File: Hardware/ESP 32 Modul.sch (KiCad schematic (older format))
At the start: 23 parts, among them U401 ESP32-WROOM-32U

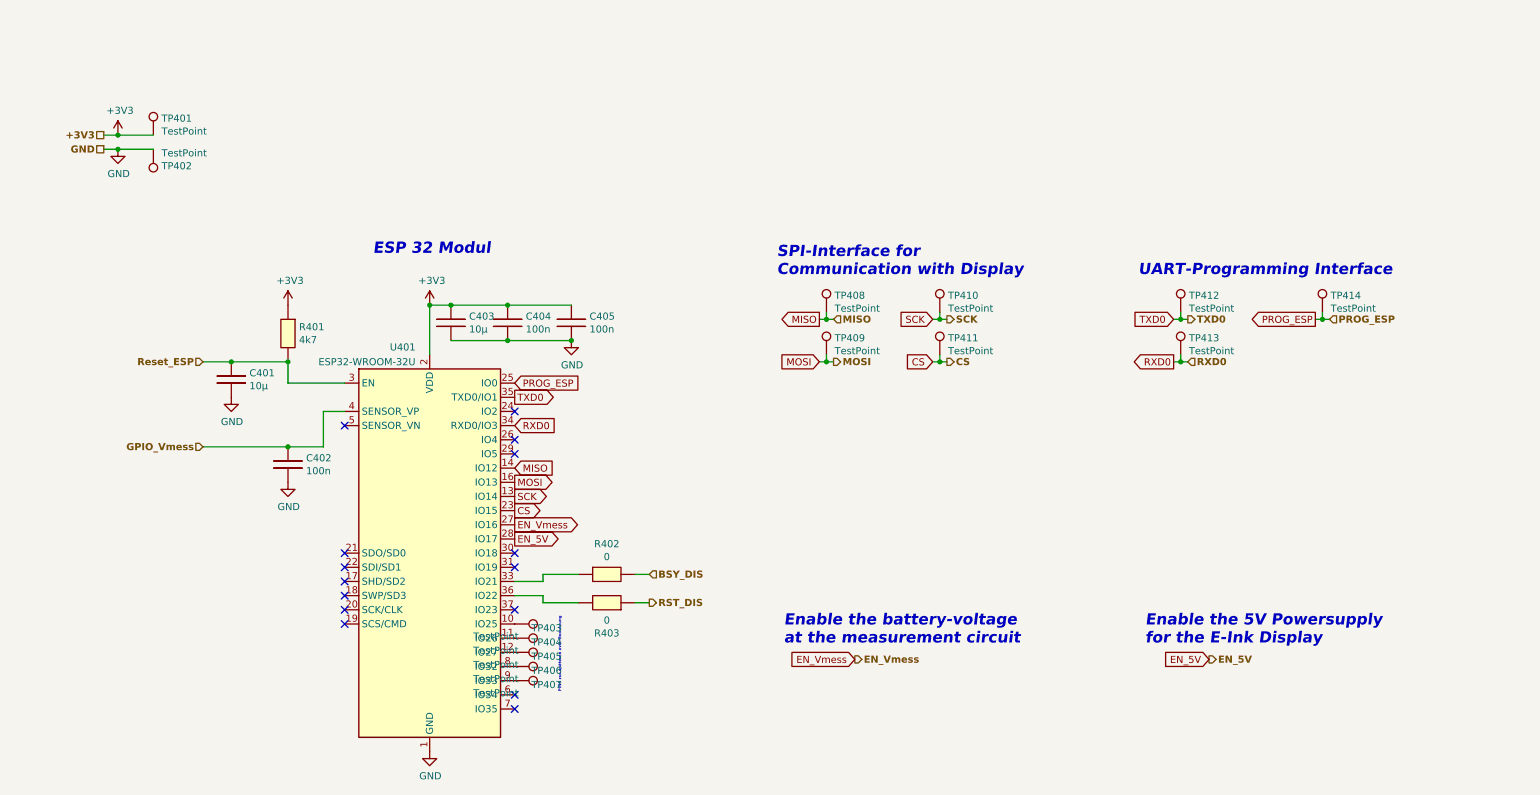
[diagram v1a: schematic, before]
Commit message: Added new MCU and redesigned schematics
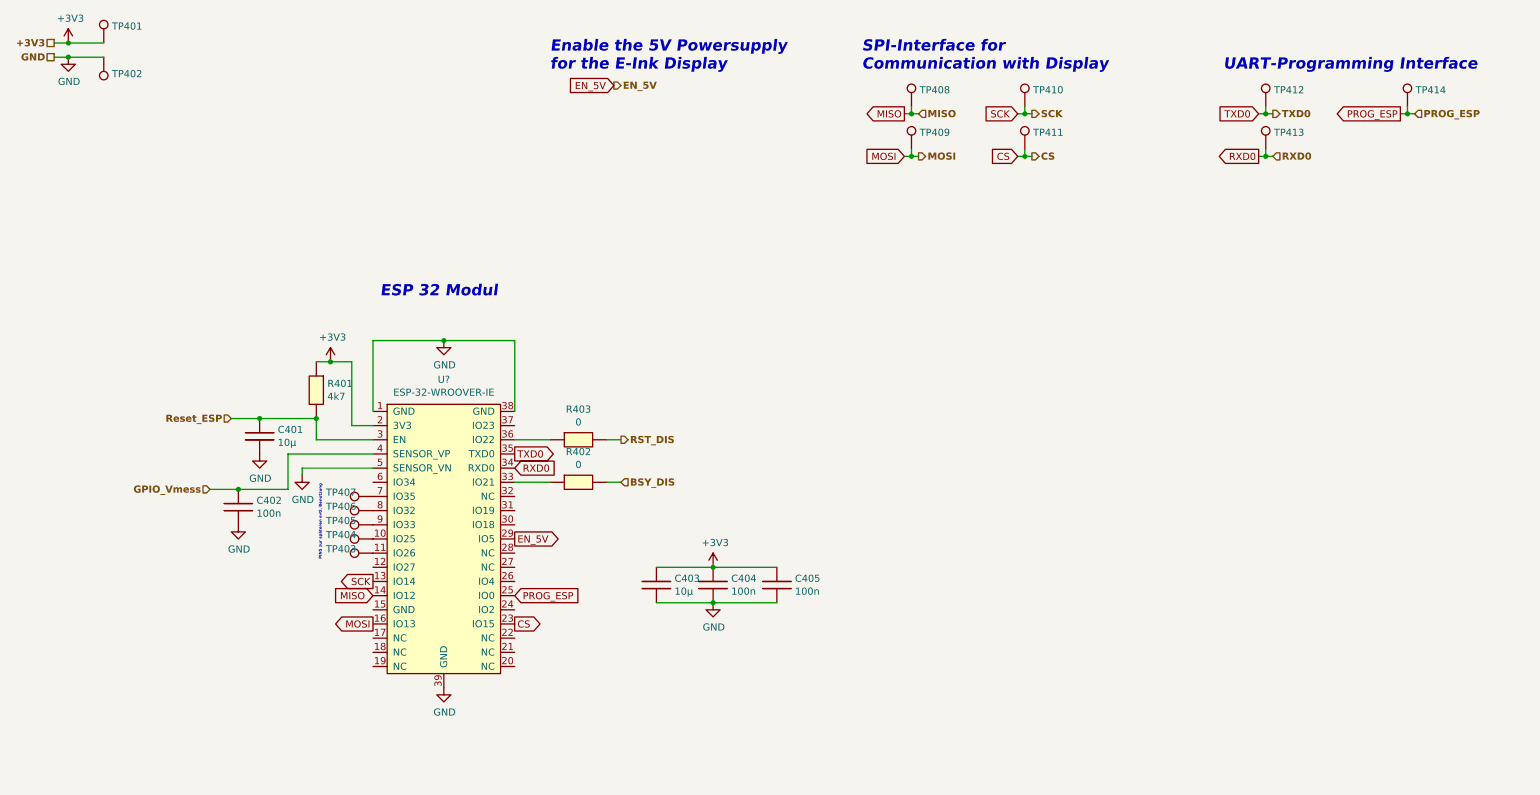
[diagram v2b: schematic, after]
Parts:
- removed U401: ESP32-WROOM-32U, RF_Module:ESP32-WROOM-32U, symbol E-Ink:ESP32-WROOM-32U
- added U?: ESP-32-WROOVER-IE, E-Ink:ESP32-WROVER, symbol E-Ink:ESP-32-WROOVER-IE
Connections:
- net +3V3: now also U?.2 (3V3)
- net CS: now also U?.23 (IO15)
- net EN_5V: now also U?.29 (IO5)
- net GND: now also U?.1 (GND), U?.38 (GND), U?.39 (GND), U?.5 (SENSOR_VN)
- net GPIO_Vmess: now also U?.4 (SENSOR_VP)
- net MISO: now also U?.14 (IO12)
- net MOSI: now also U?.16 (IO13)
- net PROG_ESP: now also U?.25 (IO0)
- net RST_DIS: now also R403.2; no longer R403.1
- net RXD0: now also U?.34 (RXD0)
- net Reset_ESP: now also U?.3 (EN)
- net SCK: now also U?.13 (IO14)
- net TXD0: now also U?.35 (TXD0)
- net at R402.1: now also U?.33 (IO21)
- net at TP403.1: now also U?.11 (IO26)
- net at TP404.1: now also U?.10 (IO25)
- net at TP405.1: now also U?.9 (IO33)
- net at TP406.1: now also U?.8 (IO32)
- net at TP407.1: now also U?.7 (IO35)
- new net: R403.1, U?.36 (IO22)
- no-connect marks 15 -> 0
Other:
- note removed: "Enable the battery-voltage \nat the measurement circuit\n"
- moved on the sheet: C401, C402, C403, C404, C405, R401, R402, R403, TP401, TP402, TP403, TP404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

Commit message: finished PCB, Thursday Review with Lukas
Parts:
- removed R402, R403: 0, Resistor_SMD:R_0805_2012Metric_Pad1.15x1.40mm_HandSolder, symbol E-Ink:0
- gave numbers to parts that had none: 1
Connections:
- net BSY_DIS: now also U401.33 (IO21)
- net RST_DIS: now also U401.36 (IO22)
- no-connect marks 0 -> 17
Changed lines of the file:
@@
 Text HLabel 4900 3950 2    50   Input ~ 10
 BSY_DIS
-Wire Wire Line
-	4800 3950 4900 3950
-Wire Wire Line
-	4400 3950 4150 3950
 Text HLabel 4900 3650 2    50   Output ~ 10
 RST_DIS
-Wire Wire Line
-	4900 3650 4800 3650
-Wire Wire Line
-	4400 3650 4150 3650
 Text GLabel 4150 4350 2    50   Output ~ 0
 EN_5V
@@
 P 3650 5400
 AR Path="/5F9351FB" Ref="#PWR?"  Part="1"
-AR Path="/5DE5A7F7/5F9351FB" Ref="#PWR?"  Part="1"
-F 0 "#PWR?" H 3650 5150 50  0001 C CNN
+AR Path="/5DE5A7F7/5F9351FB" Ref="#PWR0113"  Part="1"
+F 0 "#PWR0113" H 3650 5150 50  0001 C CNN
 F 1 "GND" H 3655 5227 50  0000 C CNN
 F 2 "" H 3650 5400 50  0001 C CNN
@@
 P 3650 2950
 AR Path="/5F9307BF" Ref="#PWR?"  Part="1"
-AR Path="/5DE5A7F7/5F9307BF" Ref="#PWR?"  Part="1"
-F 0 "#PWR?" H 3650 2700 50  0001 C CNN
+AR Path="/5DE5A7F7/5F9307BF" Ref="#PWR0114"  Part="1"
+F 0 "#PWR0114" H 3650 2700 50  0001 C CNN
 F 1 "GND" H 3655 2777 50  0000 C CNN
 F 2 "" H 3650 2950 50  0001 C CNN
@@
 P 5550 4550
 AR Path="/5F9222EC" Ref="#PWR?"  Part="1"
-AR Path="/5DE5A7F7/5F9222EC" Ref="#PWR?"  Part="1"
-F 0 "#PWR?" H 5550 4400 50  0001 C CNN
+AR Path="/5DE5A7F7/5F9222EC" Ref="#PWR0115"  Part="1"
+F 0 "#PWR0115" H 5550 4400 50  0001 C CNN
 F 1 "+3V3" H 5565 4723 50  0000 C CNN
 F 2 "" H 5550 4550 50  0001 C CNN
@@
 P 5550 4800
 AR Path="/5F91C8B0" Ref="#PWR?"  Part="1"
-AR Path="/5DE5A7F7/5F91C8B0" Ref="#PWR?"  Part="1"
-F 0 "#PWR?" H 5550 4550 50  0001 C CNN
+AR Path="/5DE5A7F7/5F91C8B0" Ref="#PWR0116"  Part="1"
+F 0 "#PWR0116" H 5550 4550 50  0001 C CNN
 F 1 "GND" H 5555 4627 50  0000 C CNN
 F 2 "" H 5550 4800 50  0001 C CNN
@@
 P 2850 3100
 AR Path="/5F909234" Ref="#PWR?"  Part="1"
-AR Path="/5DE5A7F7/5F909234" Ref="#PWR?"  Part="1"
-F 0 "#PWR?" H 2850 2950 50  0001 C CNN
+AR Path="/5DE5A7F7/5F909234" Ref="#PWR0117"  Part="1"
+F 0 "#PWR0117" H 2850 2950 50  0001 C CNN
 F 1 "+3V3" H 2865 3273 50  0000 C CNN
 F 2 "" H 2850 3100 50  0001 C CNN
@@
 P 2350 3750
 AR Path="/5F909228" Ref="#PWR?"  Part="1"
-AR Path="/5DE5A7F7/5F909228" Ref="#PWR?"  Part="1"
-F 0 "#PWR?" H 2350 3500 50  0001 C CNN
+AR Path="/5DE5A7F7/5F909228" Ref="#PWR0118"  Part="1"
+F 0 "#PWR0118" H 2350 3500 50  0001 C CNN
 F 1 "GND" H 2355 3577 50  0000 C CNN
 F 2 "" H 2350 3750 50  0001 C CNN
@@
 P 2650 3900
 AR Path="/5F900BCE" Ref="#PWR?"  Part="1"
-AR Path="/5DE5A7F7/5F900BCE" Ref="#PWR?"  Part="1"
-F 0 "#PWR?" H 2650 3650 50  0001 C CNN
+AR Path="/5DE5A7F7/5F900BCE" Ref="#PWR0119"  Part="1"
+F 0 "#PWR0119" H 2650 3650 50  0001 C CNN
 F 1 "GND" H 2655 3727 50  0000 C CNN
 F 2 "" H 2650 3900 50  0001 C CNN
@@
 P 2200 4250
 AR Path="/5F8FEE63" Ref="#PWR?"  Part="1"
-AR Path="/5DE5A7F7/5F8FEE63" Ref="#PWR?"  Part="1"
-F 0 "#PWR?" H 2200 4000 50  0001 C CNN
+AR Path="/5DE5A7F7/5F8FEE63" Ref="#PWR0120"  Part="1"
+F 0 "#PWR0120" H 2200 4000 50  0001 C CNN
 F 1 "GND" H 2205 4077 50  0000 C CNN
 F 2 "" H 2200 4250 50  0001 C CNN
@@
 $EndComp
 $Comp
-L E-Ink:ESP-32-WROOVER-IE U?
+L E-Ink:ESP-32-WROOVER-IE U401
 U 1 1 5F8ED0F7
 P 3650 3350
-F 0 "U?" H 3650 3475 50  0000 C CNN
+F 0 "U401" H 3650 3475 50  0000 C CNN
 F 1 "ESP-32-WROOVER-IE" H 3650 3384 50  0000 C CNN
 F 2 "E-Ink:ESP32-WROVER" H 3650 3450 50  0001 C CNN
@@
 	0    -1   -1   0
 $EndComp
-$Comp
-L E-Ink:0 R402
-U 1 1 5DE5CA58
-P 4500 3900
-F 0 "R402" H 4600 4065 50  0000 C CNN
-F 1 "0" H 4600 3974 50  0000 C CNN
-F 2 "Resistor_SMD:R_0805_2012Metric_Pad1.15x1.40mm_HandSolder" H 4550 3750 50  0001 C CNN
-F 3 "" H 4500 3950 50  0001 C CNN
-	1    4500 3900
-	1    0    0    -1
-$EndComp
-$Comp
-L E-Ink:0 R403
-U 1 1 5DE609BB
-P 4500 3600
-F 0 "R403" H 4600 3765 50  0000 C CNN
-F 1 "0" H 4600 3674 50  0000 C CNN
-F 2 "Resistor_SMD:R_0805_2012Metric_Pad1.15x1.40mm_HandSolder" H 4550 3450 50  0001 C CNN
-F 3 "" H 4500 3650 50  0001 C CNN
-	1    4500 3600
-	1    0    0    -1
-$EndComp
+NoConn ~ 3150 5250
+NoConn ~ 3150 5150
+NoConn ~ 3150 5050
+NoConn ~ 3150 4850
+NoConn ~ 3150 4550
+NoConn ~ 3150 3950
+NoConn ~ 4150 3550
+NoConn ~ 4150 4050
+NoConn ~ 4150 4150
+NoConn ~ 4150 4250
+NoConn ~ 4150 4450
+NoConn ~ 4150 4550
+NoConn ~ 4150 4650
+NoConn ~ 4150 4850
+NoConn ~ 4150 5050
+NoConn ~ 4150 5150
+NoConn ~ 4150 5250
+Wire Wire Line
+	4150 3650 4900 3650
+Wire Wire Line
+	4150 3950 4900 3950
 $EndSCHEMATC
